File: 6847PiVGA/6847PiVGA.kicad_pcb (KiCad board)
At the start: 2 copper layers, 68.1 x 57.7 mm, 41 parts, among them J1 DB15_Female_HighDensity, J2 Conn_01x06_Male, U1 MC6847, U2 AD724JRZ, U3 Pico, U4 AD813, Y1 4.433620MHz

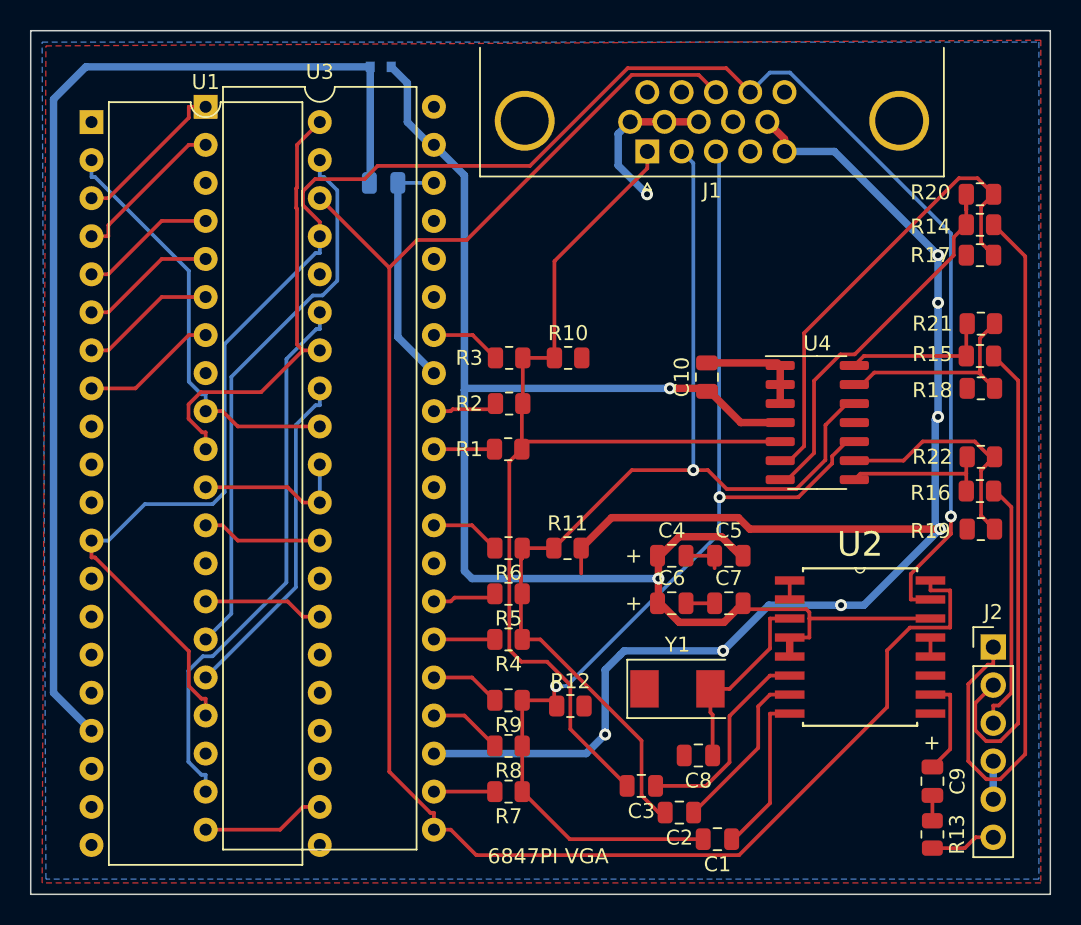
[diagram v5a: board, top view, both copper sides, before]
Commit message: add level shift
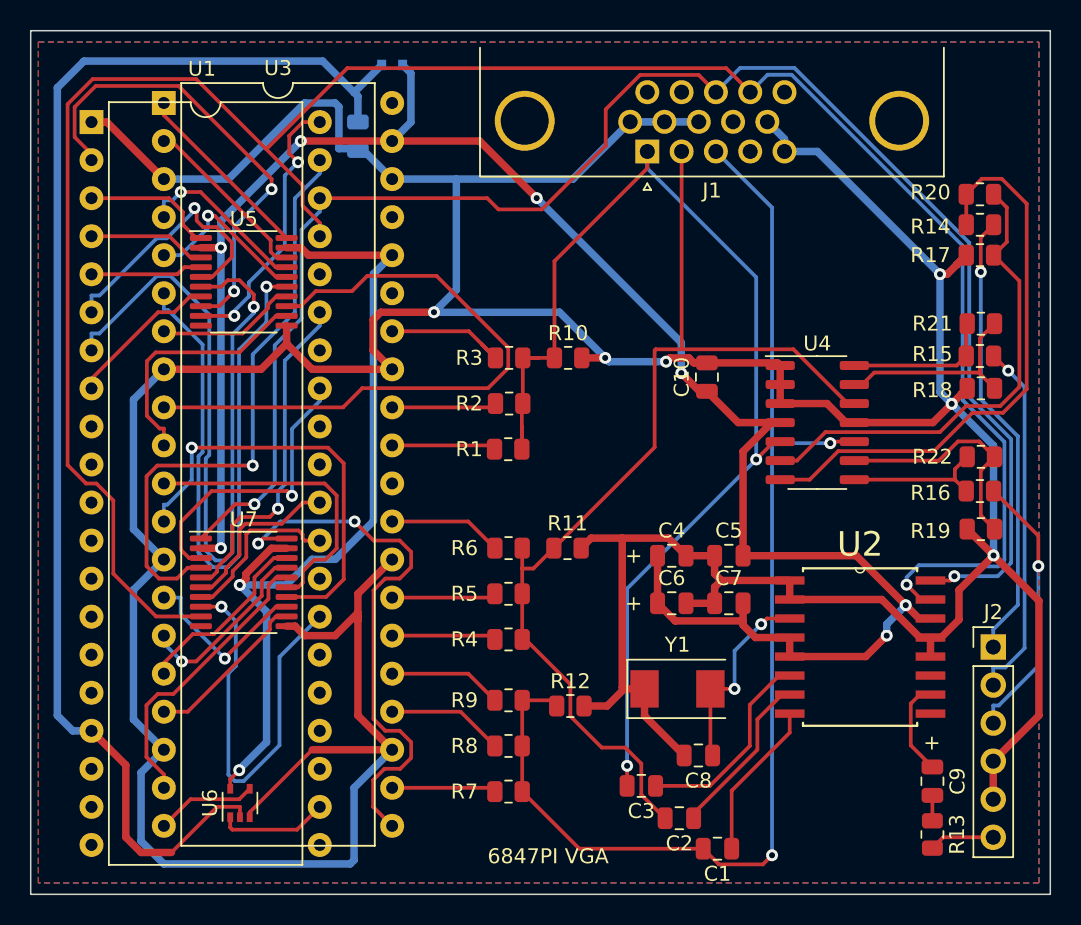
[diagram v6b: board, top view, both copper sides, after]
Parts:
- added U5: TXS0108EPW, Package_SO:TSSOP-20_4.4x6.5mm_P0.65mm, F.Cu at (93.5, 97.8)
- added U6: 2N7001T, Package_TO_SOT_SMD:SOT-353_SC-70-5, F.Cu at (93.2, 132.6)
- added U7: TXS0108EPW, Package_SO:TSSOP-20_4.4x6.5mm_P0.65mm, F.Cu at (93.5, 117.9)
- R1: value 499R -> 2K 1%
- R2: value 2K -> 1K 1%
- R3, R6, R9: value 499R -> 499R 1%
- R4, R7: value 2K -> 2K 1%
- R5, R8: value 1K -> 1K 1%
- moved C11 3.56 mm to (101.1, 88.1), turned to -90 degrees
- moved U3 2.80 mm to (88.1, 85.9)
- moved D1 0.77 mm to (103.4, 83.3)
- moved C1 0.63 mm to (125.1, 135.6)
- moved C2 0.38 mm to (122.6, 133.6)
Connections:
- U1 pad 12: Vsync -> unconnected-(U1-Pad12)
- U1 pad 31: GM0 -> unconnected-(U1-Pad31)
- U1 pad 32: DD6 -> unconnected-(U1-Pad32)
- U1 pad 33: CLK -> VCLK
- U1 pad 34: DD7 -> unconnected-(U1-Pad34)
- U3 pad 1: DD0 -> DL0
- U3 pad 10: DD7 -> DL7
- U3 pad 11: GM0 -> GM0L
- U3 pad 12: GM1 -> GM1L
- U3 pad 13: unconnected-(U3-Pad13) -> GND
- U3 pad 14: GM2 -> GM2L
- U3 pad 15: CSS -> CSSL
- U3 pad 16: CLK -> VCLKL
- U3 pad 17: Vsync -> VsyncL
- U3 pad 19: ~{A}/G -> ~{A}/G_L
- U3 pad 2: DD1 -> DL1
- U3 pad 20: Atiming -> TimingL
- U3 pad 21: Hsync -> HsyncL
- U3 pad 36: unconnected-(U3-Pad36) -> +3.3V
- U3 pad 4: DD2 -> DL2
- U3 pad 5: DD3 -> DL3
- U3 pad 6: DD4 -> DL4
- U3 pad 7: DD5 -> DL5
- U3 pad 9: DD6 -> DL6
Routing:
- net GND: track 147.7 -> 340.7 mm, vias 8 -> 6
- net +3.3V: track 0.00 -> 55.9 mm, vias 0 -> 2
- net DL6: track 0.00 -> 43.1 mm
- net DD4: track 9.10 -> 51.7 mm, vias 0 -> 1
- net DL4: track 0.00 -> 42.2 mm, vias 0 -> 1
- net HsyncL: track 0.00 -> 37.4 mm, vias 0 -> 2
- net GM1L: track 0.00 -> 28.5 mm, vias 0 -> 1
- net CLK: track 22.6 -> 0.00 mm
- net +5VD: track 106.0 -> 128.5 mm, vias 2 -> 7
- net Vsync: track 127.8 -> 149.5 mm
- net GM0L: track 0.00 -> 20.3 mm
- net VCLK: track 0.00 -> 19.8 mm, vias 0 -> 1
- net B: track 49.7 -> 30.3 mm, vias 0 -> 1
- net GM2: track 8.04 -> 27.5 mm, vias 0 -> 1
- net ~{A}/G_L: track 0.00 -> 19.4 mm
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
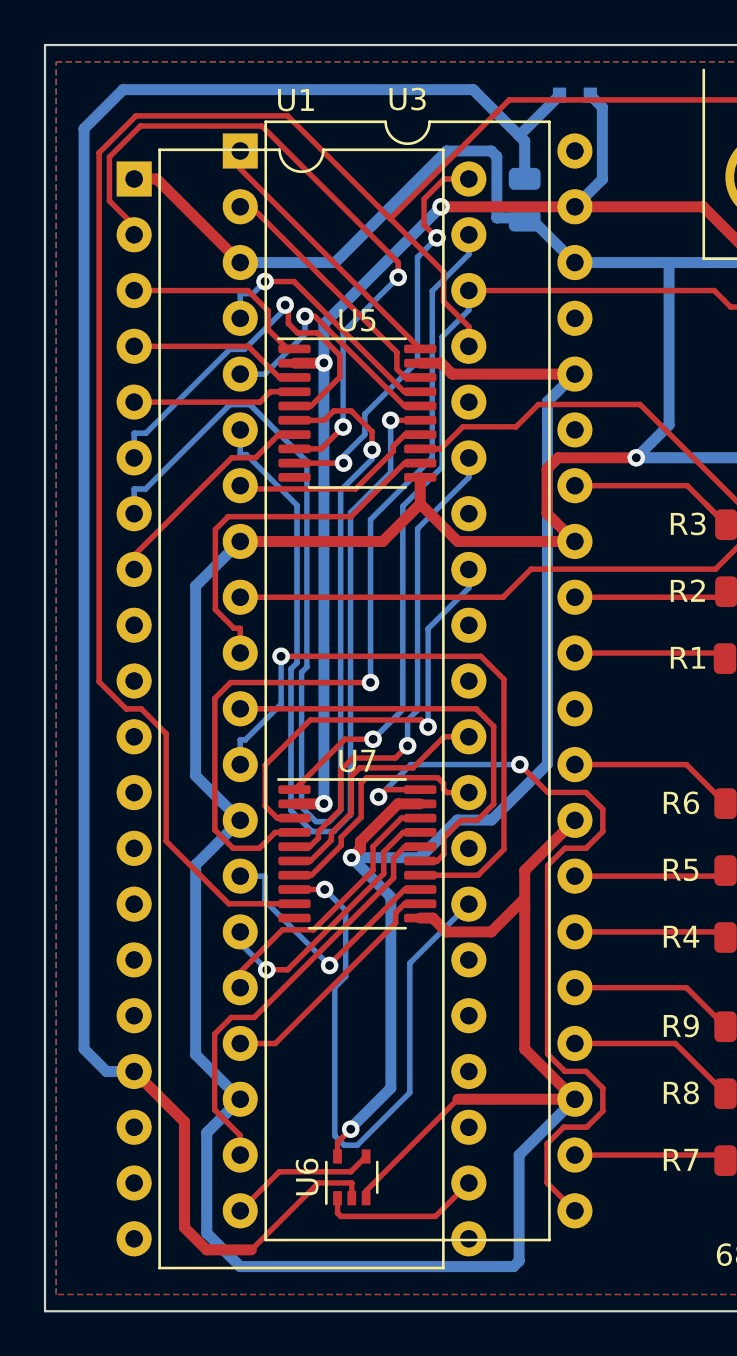
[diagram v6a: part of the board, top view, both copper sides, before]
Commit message: switch synclines from input to output
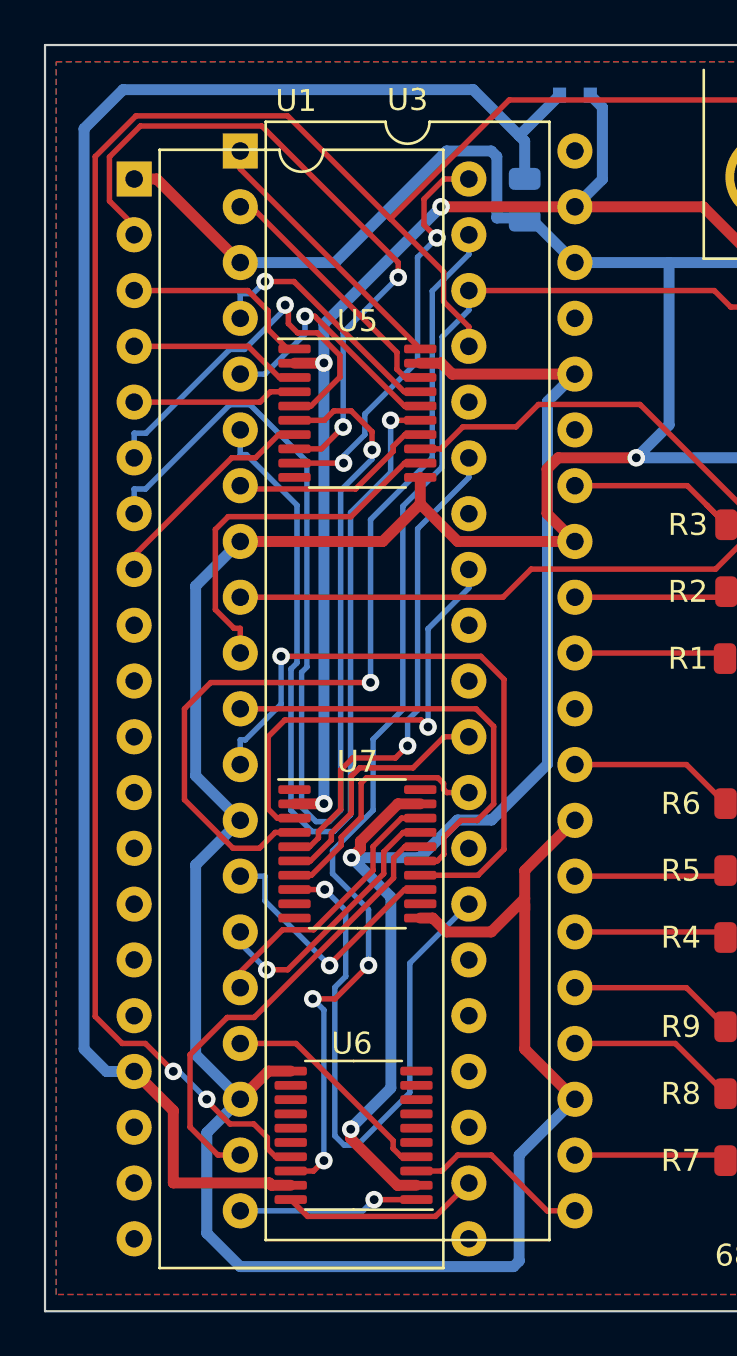
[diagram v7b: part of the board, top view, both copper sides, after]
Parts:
- U6: value 2N7001T -> TXS0108EPW; footprint Package_TO_SOT_SMD:SOT-353_SC-70-5 -> Package_SO:TSSOP-20_4.4x6.5mm_P0.65mm
- moved U6 1.92 mm to (93.3, 130.7), turned to 180 degrees
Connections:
- U6 pad 1: Atiming -> TimingL
- U6 pad 2: +5V -> +3.3V
- U6 pad 3: GND -> HsyncL
- U6 pad 4: TimingL -> VsyncL
- U6 pad 5: +3.3V -> unconnected-(U6-Pad5)
- U7 pad 1: Hsync -> unconnected-(U7-Pad1)
- U7 pad 12: VsyncL -> unconnected-(U7-Pad12)
- U7 pad 20: HsyncL -> unconnected-(U7-Pad20)
- U7 pad 9: Vsync -> unconnected-(U7-Pad9)
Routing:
- net HsyncL: track 37.4 -> 8.57 mm, vias 2 -> 0
- net Hsync: track 109.9 -> 129.6 mm, vias 2 -> 4
- net Vsync: track 149.5 -> 160.8 mm, vias 1 -> 3
- net GND: track 340.7 -> 331.9 mm
- net +5V: track 88.5 -> 81.7 mm
- net +3.3V: track 55.9 -> 58.7 mm
- net Atiming: track 7.35 -> 9.06 mm
- net CSS: track 39.9 -> 41.6 mm
- net ~{A}/G_L: track 19.4 -> 21.1 mm
- net TimingL: track 6.75 -> 8.24 mm, vias 0 -> 1
- net VsyncL: track 11.1 -> 10.4 mm
- net VCLK: track 19.8 -> 20.3 mm

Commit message: tidyup
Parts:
- added C12: 100nF, Capacitor_SMD:C_0805_2012Metric, B.Cu at (90.9, 90.9)
- added C13: 100nF, Capacitor_SMD:C_0805_2012Metric, B.Cu at (95.8, 126.0)
- added C14: 100nF, Capacitor_SMD:C_0805_2012Metric, B.Cu at (95.8, 93.0)
- added C15: 100nF, Capacitor_SMD:C_0805_2012Metric, B.Cu at (90.9, 111.8)
- added C16: 100nF, Capacitor_SMD:C_0805_2012Metric, B.Cu at (90.9, 126.0)
- added C17: 100nF, Capacitor_SMD:C_0805_2012Metric, B.Cu at (95.8, 111.8)
- added R23: 4K7, Resistor_SMD:R_0805_2012Metric, B.Cu at (101.3, 95.0)
- C4, C6: footprint Capacitor_SMD:C_0805_2012Metric -> Capacitor_SMD:C_1206_3216Metric_Pad1.33x1.80mm_HandSolder
- moved R20 2.03 mm to (142.6, 94.0)
- moved R14 2.03 mm to (142.6, 96.0)
- moved R17 2.03 mm to (142.6, 98.0)
- moved R15 1.65 mm to (142.6, 104.4)
- moved R18 1.65 mm to (142.7, 106.6)
- moved R21 1.65 mm to (142.7, 102.2)
- moved U7 1.27 mm to (93.5, 116.6)
- moved C4 0.63 mm to (121.4, 116.1)
- moved C6 0.63 mm to (121.4, 119.3)
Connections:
- J1 pad 0: (no net) -> GND
- U3 pad 20: TimingL -> HsyncL
- U3 pad 21: HsyncL -> TimingL
- U3 pad 36: +3.3V -> OE
- U5 pad 1: DD0 -> DL0
- U5 pad 10: unconnected-(U5-Pad10) -> OE
- U5 pad 12: DL7 -> DD7
- U5 pad 13: DL6 -> DD6
- U5 pad 14: DL5 -> DD5
- U5 pad 15: DL4 -> DD4
- U5 pad 16: DL3 -> DD3
- U5 pad 17: DL2 -> DD2
- U5 pad 18: DL1 -> DD1
- U5 pad 19: +3.3V -> +5VD
- U5 pad 2: +5VD -> OE
- U5 pad 20: DL0 -> DD0
- U5 pad 3: DD1 -> DL1
- U5 pad 4: DD2 -> DL2
- U5 pad 5: DD3 -> DL3
- U5 pad 6: DD4 -> DL4
- U5 pad 7: DD5 -> DL5
- U5 pad 8: DD6 -> DL6
- U5 pad 9: DD7 -> DL7
- U6 pad 10: unconnected-(U6-Pad10) -> OE
- U6 pad 19: +5V -> +5VD
- U6 pad 2: +3.3V -> OE
- U7 pad 10: unconnected-(U7-Pad10) -> OE
- U7 pad 13: GM2L -> GM2
- U7 pad 14: GM1L -> GM1
- U7 pad 15: GM0L -> GM0
- U7 pad 16: ~{A}/G_L -> ~{A}/G
- U7 pad 17: CSSL -> VCLK
- U7 pad 18: VCLKL -> CSS
- U7 pad 19: +3.3V -> +5VD
- U7 pad 2: +5VD -> OE
- U7 pad 3: VCLK -> CSSL
- U7 pad 4: CSS -> VCLKL
- U7 pad 5: ~{A}/G -> ~{A}/G_L
- U7 pad 6: GM0 -> GM0L
- U7 pad 7: GM1 -> GM1L
- U7 pad 8: GM2 -> GM2L
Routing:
- net OE: track 0.00 -> 90.1 mm, vias 0 -> 7
- net GND: track 331.9 -> 419.1 mm, vias 6 -> 9
- net +3.3V: track 58.7 -> 0.00 mm, vias 2 -> 0
- net DL4: track 42.2 -> 2.65 mm, vias 1 -> 0
- net DD4: track 51.7 -> 14.9 mm, vias 1 -> 0
- net DL6: track 43.1 -> 8.37 mm, vias 0 -> 1
- net Vsync: track 160.8 -> 133.1 mm, vias 3 -> 2
- net GM2: track 27.5 -> 3.32 mm, vias 1 -> 0
- net Atiming: track 9.06 -> 31.7 mm
- net GM1L: track 28.5 -> 7.61 mm, vias 1 -> 0
- net +5VD: track 128.5 -> 142.4 mm, vias 7 -> 10
- net +5V: track 81.7 -> 68.2 mm, vias 0 -> 1
- net CSS: track 41.6 -> 28.2 mm, vias 1 -> 0
- net DD1: track 7.89 -> 20.7 mm, vias 0 -> 1
- net DD3: track 18.0 -> 29.7 mm, vias 1 -> 4
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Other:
- board size 68.1 x 57.7 mm -> 66.3 x 57.7 mm
- board text added: "6847PI VGA Revision 3"
- board text removed: "6847PI VGA Revision 2"
